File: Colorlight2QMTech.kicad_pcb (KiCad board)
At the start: 4 copper layers, 66 x 85.7 mm, 17 parts, among them CN1 1473005-4, J1 Conn_02x32_Odd_Even, J2 Conn_02x32_Odd_Even, J3 Connector_USB_C_Receptacle_US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, J4 Conn_01x14_Male, J4-GND1 Conn_01x01_Male, J5 Conn_01x14_Male, U1 AMS1117-3.3

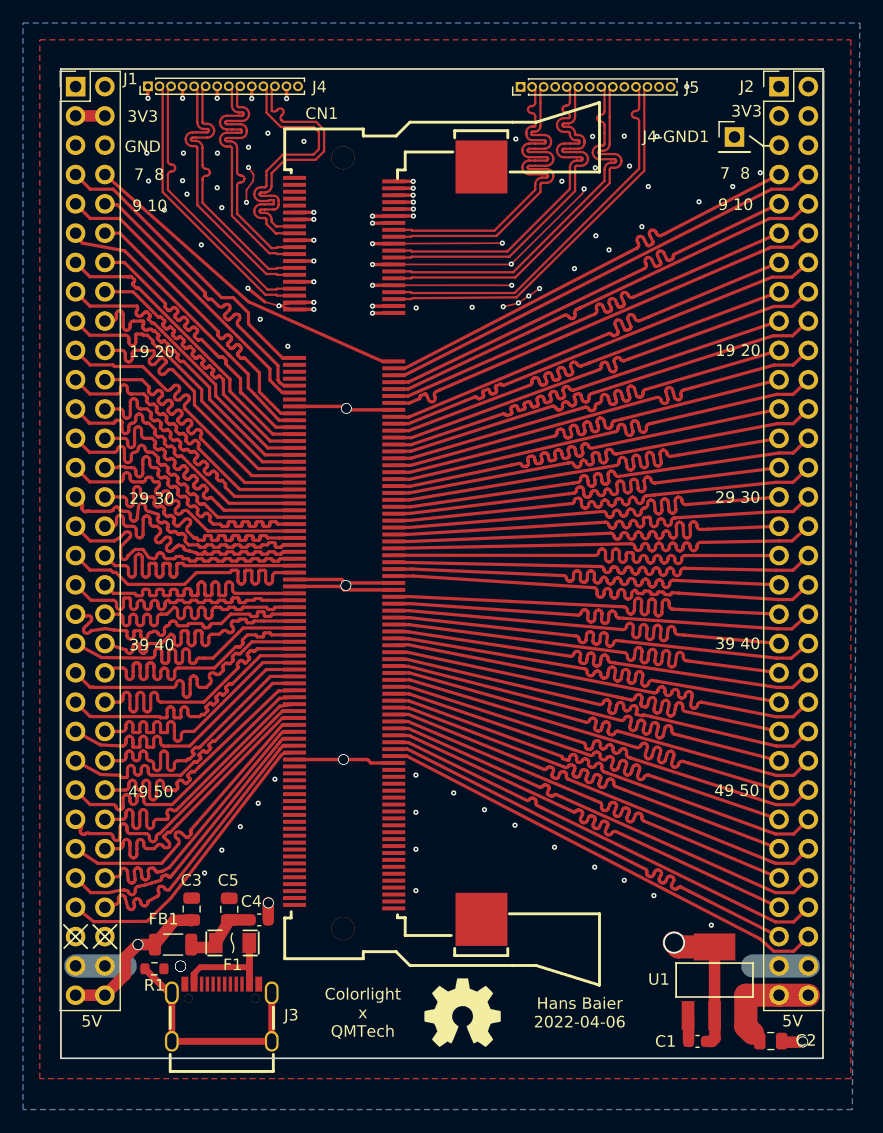
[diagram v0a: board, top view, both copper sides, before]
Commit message: regymm modified 2 layer ver.
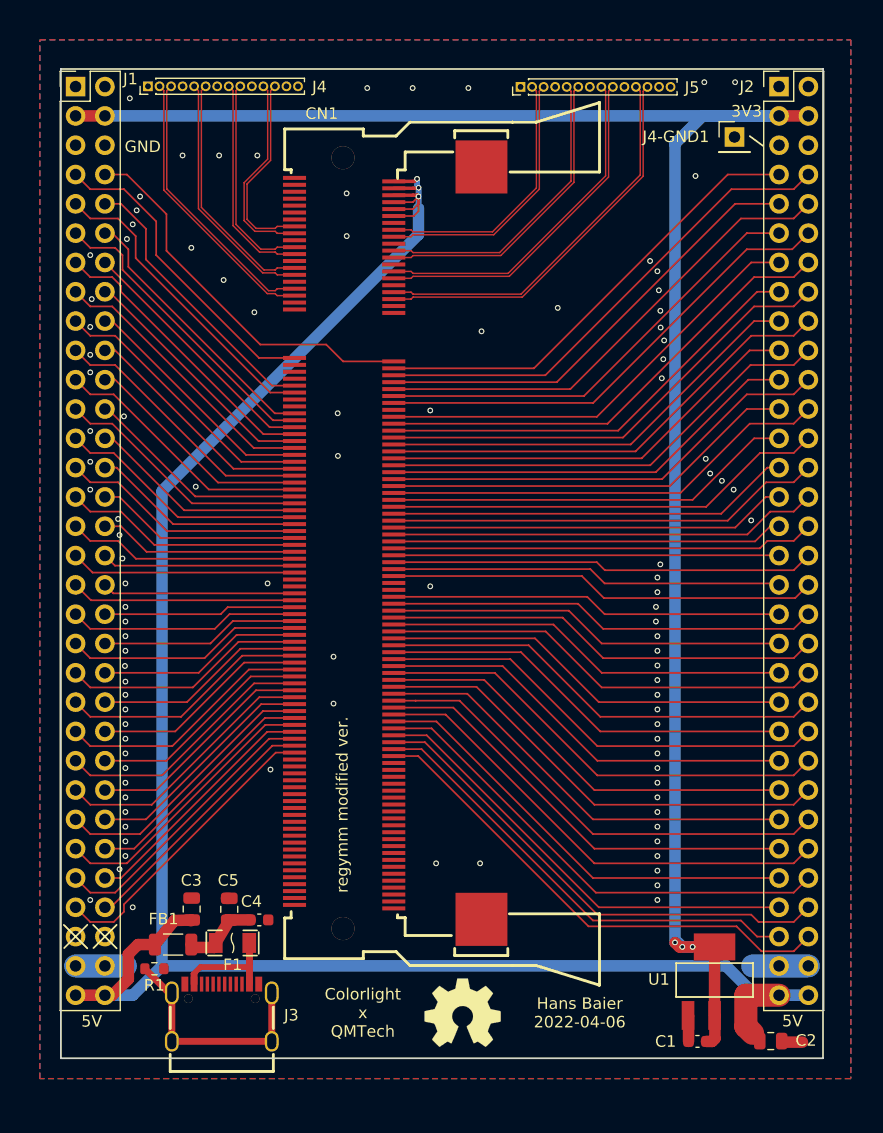
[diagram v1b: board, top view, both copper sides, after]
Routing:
- net GND: track 158.9 -> 13.2 mm, vias 88 -> 103
- net +5V: track 45.8 -> 177.2 mm, vias 8 -> 3
- net /eth2_1+: track 33.5 -> 22.9 mm
- net /eth2_1-: track 33.6 -> 23.3 mm
- net /eth1_1+: track 27.1 -> 17.0 mm
- net /eth1_1-: track 27.2 -> 17.5 mm
- net /E19: track 26.1 -> 16.7 mm
- net /F19: track 26.1 -> 16.8 mm
- net /D19: track 25.9 -> 16.7 mm
- net /B20: track 26.1 -> 17.2 mm
- net /G19: track 26.2 -> 17.3 mm
- net /B18: track 26.2 -> 17.8 mm
- net /H20: track 26.1 -> 17.9 mm
- net /C17: track 26.2 -> 18.3 mm
- net /J20: track 26.0 -> 18.5 mm
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- removed copper zone on In2.Cu, net +5V
- removed copper zone on In1.Cu, net GND
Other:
- copper layers 4 -> 2
- board text added: "regymm modified ver."
- board text removed: "19 20"
- board text removed: "29 30"
- board text removed: "39 40"
- board text removed: "49 50"
- board text removed: "7 8"
- board text removed: "9 10"
